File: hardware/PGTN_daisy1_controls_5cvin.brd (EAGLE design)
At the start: 69.9 x 110.5 mm, 86 parts, among them J1 HEADER/MALE/01, J2 HEADER/MALE/01

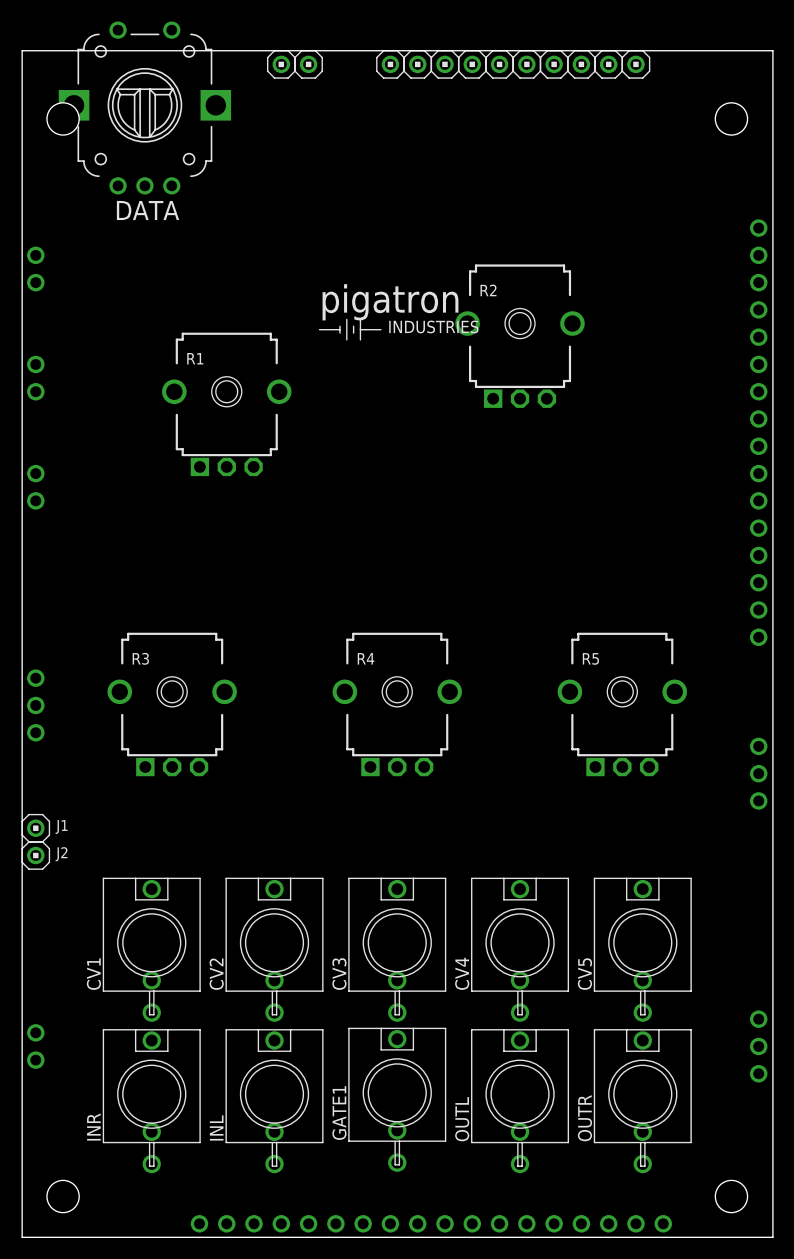
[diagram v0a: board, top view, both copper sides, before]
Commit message: Moved UI handling out of controllers
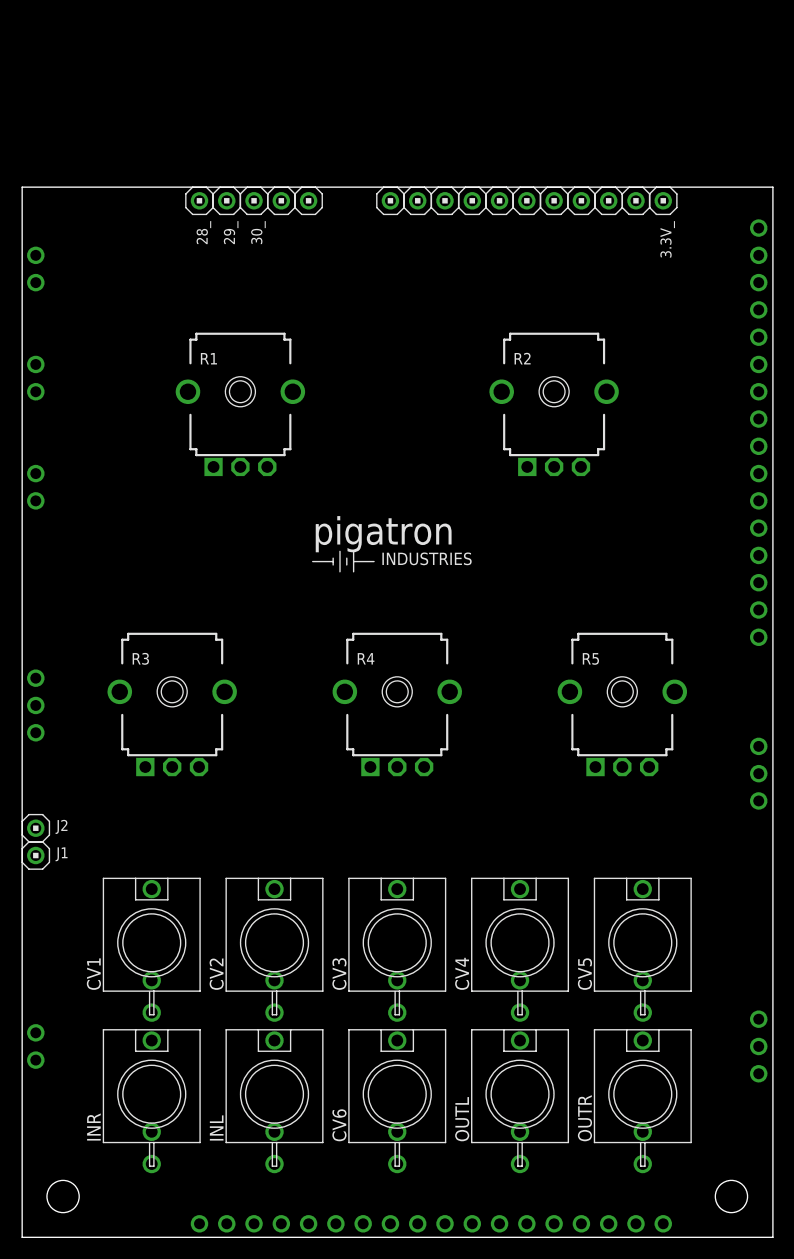
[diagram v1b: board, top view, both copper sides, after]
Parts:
- removed DATA: ENCODER_SW1-PEC12, controls:PEC12_INCREMENTAL_ENCODER
- removed GATE1: WQP-PJ301M-12_JACK, controls:WQP-PJ301M-12_JACK
- removed U$4, U$7: (no value), mechanical:STANDOFF/3.0
- added 28_, 29_, 3.3V_, 30_: HEADER/MALE/01, connectors:HEADER/MALE/01
- added CV6: WQP-PJ301M-12_JACK, controls:WQP-PJ301M-12_JACK
- moved U$1 21.6 mm to (35.9, 64.5)
- moved 10_MOSI_ 12.7 mm to (34.3, 96.5)
- moved 13_TX_ 12.7 mm to (26.7, 96.5)
- moved 14_RX_ 12.7 mm to (24.1, 96.5)
- moved 1_SD_D3_ 12.7 mm to (57.1, 96.5)
- moved 2_SD_D2_ 12.7 mm to (54.6, 96.5)
- moved 3_SD_D1_ 12.7 mm to (52.1, 96.5)
- moved 4_SD_D0_ 12.7 mm to (49.5, 96.5)
- moved 5_SD_CMD_ 12.7 mm to (47.0, 96.5)
- moved 6_SD_CLK_ 12.7 mm to (44.5, 96.5)
- moved 7_CS_ 12.7 mm to (41.9, 96.5)
- moved 8_SCK_ 12.7 mm to (39.4, 96.5)
- moved 9_MISO_ 12.7 mm to (36.8, 96.5)
- moved R2 7.10 mm to (49.5, 78.7)
- moved J1 2.54 mm to (1.27, 35.6)
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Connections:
- removed net N$25: 30.1, DATA.A
- removed net N$26: 29.1, DATA.B
- removed net N$27: 28.1, DATA.P1
- removed net N$32: GATE1.P$2, J1.1
- new net N$10: CV6.P$1, CV6A.1
- new net N$11: CV6.P$2, J1.1
- new net N$12: 28.1, 28_.1
- new net N$14: 29.1, 29_.1
- new net N$18: 30.1, 30_.1
- new net N$19: 3.3V.1, 3.3V_.1
- net N$13: no longer GATE1.P$1
- net PE: now also CV6.P$3; no longer DATA.C, DATA.P2, GATE1.P$3
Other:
- board size 69.9 x 110.5 mm -> 69.9 x 97.8 mm
